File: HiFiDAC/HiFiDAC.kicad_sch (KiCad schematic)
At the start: 1 part, among them U2 PCM1794A

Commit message: HiFiDAC progress
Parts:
- added C27, C28, C29, C30, C31, C32: 47µF 20V, symbol Device:C_Polarized_Small
- added C33, C34, C35, C36: 0.1µF C0G, symbol Device:C_Small
- added C37: 1µF, symbol Device:C_Small
- added J1: I2S, symbol Connector:Conn_01x05_Pin
- added J2: Conn_01x04_Pin, symbol Connector:Conn_01x04_Pin
- added JP1: SolderJumper_2_Open, Jumper:SolderJumper-2_P1.3mm_Open_RoundedPad1.0x1.5mm, symbol Jumper:SolderJumper_2_Open
- added R31: 10kΩLN, symbol Device:R_US
- added R32: 10Ω, symbol Device:R_US
- added R33, R34, R35, R36, R38: 27Ω, symbol Device:R_US
- added R37: 1kΩ, symbol Device:R_US
- added R39: 100kΩ, symbol Device:R_US
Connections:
- net I-V Stage/IL+: now also U2.25 (IOUTL+)
- net I-V Stage/IL-: now also U2.26 (IOUTL-)
- net I-V Stage/IR+: now also U2.17 (IOUTR+)
- net I-V Stage/IR-: now also U2.18 (IOUTR-)
- net at U2.10 (MUTE): now also R36.2
- net ZERO: now reaches U2.13 (ZERO)
- net ZERO: now also R38.2
- net at U2.14 (~{RST}): now also C37.1, R37.2, R39.1
- net +5V: now reaches U2.15 (VCC2R)
- net +5V: now also U2.23 (VCC1), U2.28 (VCC2L), C27.1, C28.1, C29.1, C30.1, C31.1, C33.2, C34.2, C35.2
- net GND: now reaches U2.16 (AGND3R)
- net GND: now also U2.19 (AGND1), U2.24 (AGND2), U2.27 (AGND3L), U2.8 (DGND), C29.2, C30.2, C31.2, C32.2, C33.1, C34.1, C35.1, C36.2, C37.2, J1.1 (Pin_1), J2.4 (Pin_4), R31.2, R39.2
- net at U2.20 (IREF): now also R31.1
- net at U2.21 (VCOMR): now also C28.2
- net at U2.22 (VCOML): now also C27.2
- net at U2.4 (LRCK): now also R34.2
- net at U2.5 (DATA): now also R35.2
- net at U2.6 (BCK): now also R33.2
- net at U2.7 (SCK): now also R32.2
- net +3.3V: now reaches U2.9 (VDD)
- net +3.3V: now also C32.1, C36.1
- new net: J2.3 (Pin_3), R38.1
- new net: J1.4 (Pin_4), R34.1
- new net: J2.1 (Pin_1), R36.1
- new net: J2.2 (Pin_2), R37.1
- new net: J1.2 (Pin_2), R32.1
- new net: J1.3 (Pin_3), R33.1
- new net: J1.5 (Pin_5), R35.1
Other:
- moved on the sheet: U2

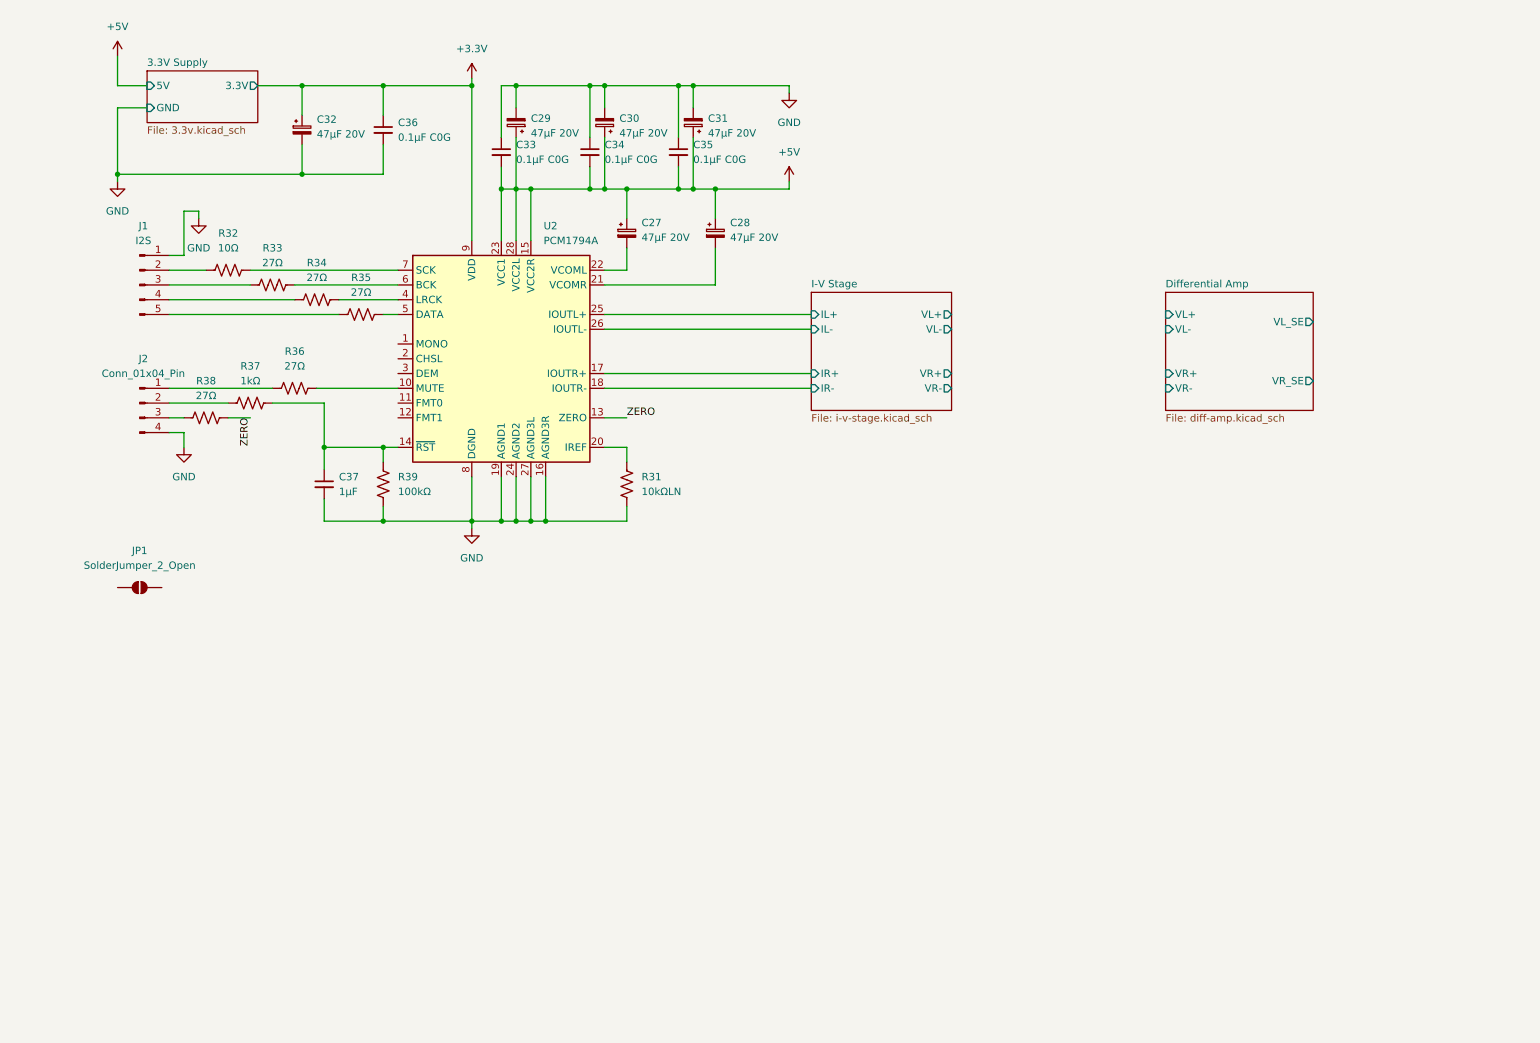
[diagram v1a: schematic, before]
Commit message: HiFiDAC schematic initially done, CleanLVSupply added shield pads
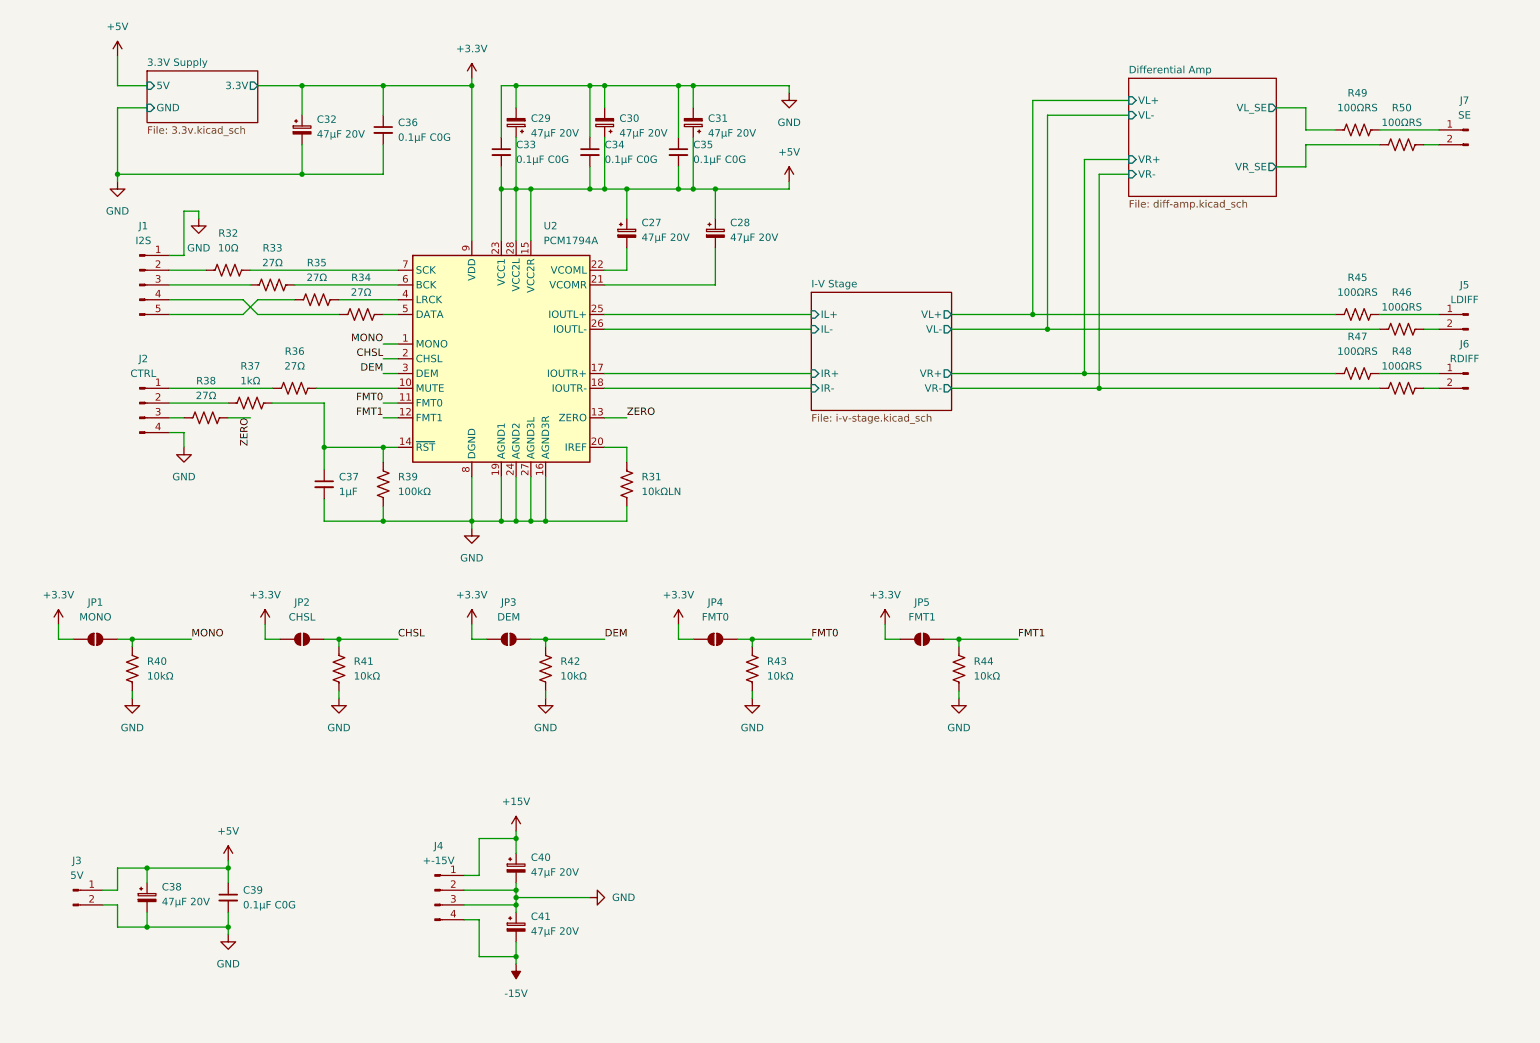
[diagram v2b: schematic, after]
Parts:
- added C38, C40, C41: 47µF 20V, symbol Device:C_Polarized_Small
- added C39: 0.1µF C0G, symbol Device:C_Small
- added J3: 5V, symbol Connector:Conn_01x02_Pin
- added J4: +-15V, symbol Connector:Conn_01x04_Pin
- added J5: LDIFF, symbol Connector:Conn_01x02_Pin
- added J6: RDIFF, symbol Connector:Conn_01x02_Pin
- added J7: SE, symbol Connector:Conn_01x02_Pin
- added JP2: CHSL, Jumper:SolderJumper-2_P1.3mm_Open_RoundedPad1.0x1.5mm, symbol Jumper:SolderJumper_2_Open
- added JP3: DEM, Jumper:SolderJumper-2_P1.3mm_Open_RoundedPad1.0x1.5mm, symbol Jumper:SolderJumper_2_Open
- added JP4: FMT0, Jumper:SolderJumper-2_P1.3mm_Open_RoundedPad1.0x1.5mm, symbol Jumper:SolderJumper_2_Open
- added JP5: FMT1, Jumper:SolderJumper-2_P1.3mm_Open_RoundedPad1.0x1.5mm, symbol Jumper:SolderJumper_2_Open
- added R40, R41, R42, R43, R44: 10kΩ, symbol Device:R_US
- added R45, R46, R47, R48, R49, R50: 100ΩRS, symbol Device:R_US
- J2: value Conn_01x04_Pin -> CTRL
- JP1: value SolderJumper_2_Open -> MONO
- renumbered R35 to R34, R34 to R35
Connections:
- net +3.3V: now also JP1.1 (A), JP2.1 (A), JP3.1 (A), JP4.1 (A), JP5.1 (A)
- net +5V: now also C38.1, C39.1, J3.1 (Pin_1)
- net Differential Amp/VL+: now also R45.2
- net Differential Amp/VL-: now also R46.2
- net Differential Amp/VL_SE: now also R49.2
- net Differential Amp/VR+: now also R47.2
- net Differential Amp/VR-: now also R48.2
- net Differential Amp/VR_SE: now also R50.2
- net GND: now also C38.2, C39.2, C40.2, C41.1, J3.2 (Pin_2), J4.2 (Pin_2), J4.3 (Pin_3), R40.2, R41.2, R42.2, R43.2, R44.2
- net MONO: now reaches JP1.2 (B)
- net MONO: now also U2.1 (MONO), R40.1
- net at R35.1: now also J1.5 (Pin_5); no longer J1.4 (Pin_4)
- net at R34.1: now also J1.4 (Pin_4); no longer J1.5 (Pin_5)
- net FMT0: now reaches U2.11 (FMT0)
- net FMT0: now also JP4.2 (B), R43.1
- net FMT1: now reaches U2.12 (FMT1)
- net FMT1: now also JP5.2 (B), R44.1
- net CHSL: now reaches U2.2 (CHSL)
- net CHSL: now also JP2.2 (B), R41.1
- net DEM: now reaches U2.3 (DEM)
- net DEM: now also JP3.2 (B), R42.1
- new net: J5.1 (Pin_1), R45.1
- new net: J5.2 (Pin_2), R46.1
- new net: J6.1 (Pin_1), R47.1
- new net: J6.2 (Pin_2), R48.1
- new net: J7.1 (Pin_1), R49.1
- new net: J7.2 (Pin_2), R50.1
- new net +15V: C40.1, J4.1 (Pin_1)
- new net -15V: C41.2, J4.4 (Pin_4)
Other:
- moved on the sheet: JP1

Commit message: HiFiDAC renumbered and footprints assigned
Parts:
- C1: renamed from C29; footprint (none) -> Capacitor_SMD:CP_Elec_5x5.8
- C10: renamed from C28; footprint (none) -> Capacitor_SMD:CP_Elec_5x5.8
- C11: renamed from C37; footprint (none) -> Capacitor_SMD:C_0603_1608Metric
- C12: renamed from C40; footprint (none) -> Capacitor_SMD:CP_Elec_5x5.8
- C13: renamed from C38; footprint (none) -> Capacitor_SMD:CP_Elec_5x5.8
- C14: renamed from C39; footprint (none) -> BW_PassiveMechanical:C_0704_1810Metric
- C15: renamed from C41; footprint (none) -> Capacitor_SMD:CP_Elec_5x5.8
- C2: renamed from C30; footprint (none) -> Capacitor_SMD:CP_Elec_5x5.8
- C3: renamed from C31; footprint (none) -> Capacitor_SMD:CP_Elec_5x5.8
- C4: renamed from C32; footprint (none) -> Capacitor_SMD:CP_Elec_5x5.8
- C5: renamed from C36; footprint (none) -> BW_PassiveMechanical:C_0704_1810Metric
- C6: renamed from C33; footprint (none) -> BW_PassiveMechanical:C_0704_1810Metric
- C7: renamed from C34; footprint (none) -> BW_PassiveMechanical:C_0704_1810Metric
- C8: renamed from C35; footprint (none) -> BW_PassiveMechanical:C_0704_1810Metric
- C9: renamed from C27; footprint (none) -> Capacitor_SMD:CP_Elec_5x5.8
- J1: renamed from J7; footprint (none) -> BW_Connectors:Amphenol_MINITEK_0.8_2P_V
- J2: renamed from J1; footprint (none) -> BW_Connectors:Amphenol_MINITEK_0.8_5P_V
- J3: renamed from J5; footprint (none) -> BW_Connectors:Amphenol_MINITEK_0.8_2P_V
- J4: renamed from J6; footprint (none) -> BW_Connectors:Amphenol_MINITEK_0.8_2P_V
- J5: renamed from J2; footprint (none) -> BW_Connectors:Amphenol_MINITEK_0.8_4P_V
- J6: renamed from J3; footprint (none) -> BW_Connectors:Amphenol_MINITEK_0.8_2P_V
- J7: renamed from J4; footprint (none) -> BW_Connectors:Amphenol_MINITEK_0.8_4P_V
- R1: renamed from R49; footprint (none) -> Resistor_SMD:R_0805_2012Metric
- R10: renamed from R36; footprint (none) -> Resistor_SMD:R_0603_1608Metric
- R11: renamed from R48; footprint (none) -> Resistor_SMD:R_0805_2012Metric
- R12: renamed from R37; footprint (none) -> Resistor_SMD:R_0603_1608Metric
- R13: renamed from R38; footprint (none) -> Resistor_SMD:R_0603_1608Metric
- R14: renamed from R39; footprint (none) -> Resistor_SMD:R_0603_1608Metric
- R15: renamed from R31; footprint (none) -> Resistor_SMD:R_0603_1608Metric
- R16: renamed from R40; footprint (none) -> Resistor_SMD:R_0603_1608Metric
- R17: renamed from R41; footprint (none) -> Resistor_SMD:R_0603_1608Metric
- R18: renamed from R42; footprint (none) -> Resistor_SMD:R_0603_1608Metric
- R19: renamed from R43; footprint (none) -> Resistor_SMD:R_0603_1608Metric
- R2: renamed from R50; footprint (none) -> Resistor_SMD:R_0805_2012Metric
- R20: renamed from R44; footprint (none) -> Resistor_SMD:R_0603_1608Metric
- R3: renamed from R32; footprint (none) -> Resistor_SMD:R_0603_1608Metric
- R4: renamed from R33; footprint (none) -> Resistor_SMD:R_0603_1608Metric
- R5: renamed from R35; footprint (none) -> Resistor_SMD:R_0603_1608Metric
- R6: renamed from R34; footprint (none) -> Resistor_SMD:R_0603_1608Metric
- R7: renamed from R45; footprint (none) -> Resistor_SMD:R_0805_2012Metric
- R8: renamed from R46; footprint (none) -> Resistor_SMD:R_0805_2012Metric
- R9: renamed from R47; footprint (none) -> Resistor_SMD:R_0805_2012Metric
- renumbered U2 to U1

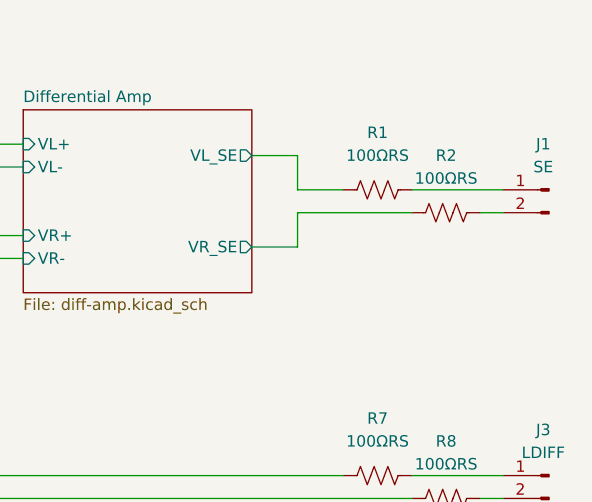
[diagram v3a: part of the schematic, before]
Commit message: HiFiDAC PCB progress, slight shape changes
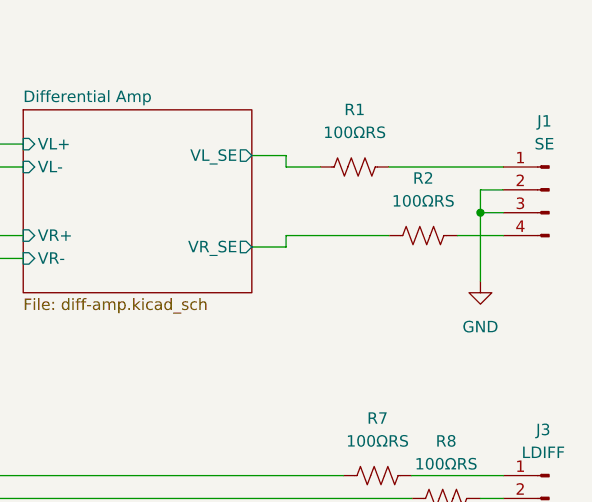
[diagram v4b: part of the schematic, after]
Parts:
- J1: footprint BW_Connectors:Amphenol_MINITEK_0.8_2P_V -> BW_Connectors:Amphenol_MINITEK_0.8_4P_V; symbol Connector:Conn_01x02_Pin -> Connector:Conn_01x04_Pin
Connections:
- net GND: now also J1.2 (Pin_2), J1.3 (Pin_3)
- net at R2.1: now also J1.4 (Pin_4); no longer J1.2 (Pin_2)
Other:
- moved on the sheet: R1, R2
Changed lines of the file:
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@@
 	)
 	(junction
+		(at 264.16 39.37)
+		(diameter 0)
+		(color 0 0 0 0)
+	)
+	(junction
 		(at 120.65 29.21)
 		(diameter 0)
@@
 	(wire
 		(pts
-			(xy 243.84 36.83) (xy 243.84 33.02)
+			(xy 242.57 34.29) (xy 242.57 33.02)
 		)
 		(stroke
@@
 	(wire
 		(pts
+			(xy 264.16 39.37) (xy 264.16 46.99)
+		)
+		(stroke
+			(width 0)
+			(type default)
+		)
+	)
+	(wire
+		(pts
 			(xy 101.6 172.72) (xy 101.6 179.07)
 		)
@@
 	(wire
 		(pts
+			(xy 261.62 41.91) (xy 266.7 41.91)
+		)
+		(stroke
+			(width 0)
+			(type default)
+		)
+	)
+	(wire
+		(pts
 			(xy 107.95 29.21) (xy 107.95 33.02)
 		)
@@
 	(wire
 		(pts
-			(xy 58.42 162.56) (xy 58.42 163.83)
+			(xy 266.7 36.83) (xy 264.16 36.83)
 		)
 		(stroke
@@
 	(wire
 		(pts
-			(xy 120.65 43.18) (xy 120.65 46.99)
+			(xy 58.42 162.56) (xy 58.42 163.83)
 		)
 		(stroke
@@
 	(wire
 		(pts
-			(xy 264.16 39.37) (xy 266.7 39.37)
+			(xy 120.65 43.18) (xy 120.65 46.99)
 		)
 		(stroke
@@
 	(wire
 		(pts
-			(xy 248.92 36.83) (xy 243.84 36.83)
+			(xy 246.38 34.29) (xy 242.57 34.29)
 		)
 		(stroke
@@
 	(wire
 		(pts
+			(xy 264.16 39.37) (xy 266.7 39.37)
+		)
+		(stroke
+			(width 0)
+			(type default)
+		)
+	)
+	(wire
+		(pts
 			(xy 105.41 46.99) (xy 105.41 55.88)
 		)
@@
 	(wire
 		(pts
+			(xy 264.16 36.83) (xy 264.16 39.37)
+		)
+		(stroke
+			(width 0)
+			(type default)
+		)
+	)
+	(wire
+		(pts
 			(xy 100.33 121.92) (xy 100.33 124.46)
 		)
@@
 	(wire
 		(pts
-			(xy 243.84 39.37) (xy 256.54 39.37)
+			(xy 242.57 41.91) (xy 254 41.91)
 		)
 		(stroke
@@
 	(wire
 		(pts
-			(xy 238.76 43.18) (xy 243.84 43.18)
+			(xy 238.76 43.18) (xy 242.57 43.18)
 		)
 		(stroke
@@
 	(wire
 		(pts
-			(xy 256.54 36.83) (xy 266.7 36.83)
-		)
-		(stroke
-			(width 0)
-			(type default)
-		)
-	)
-	(wire
-		(pts
 			(xy 100.33 104.14) (xy 105.41 104.14)
 		)
@@
 	(wire
 		(pts
-			(xy 243.84 43.18) (xy 243.84 39.37)
+			(xy 242.57 43.18) (xy 242.57 41.91)
 		)
 		(stroke
@@
 	(wire
 		(pts
+			(xy 254 34.29) (xy 266.7 34.29)
+		)
+		(stroke
+			(width 0)
+			(type default)
+		)
+	)
+	(wire
+		(pts
 			(xy 135.89 121.92) (xy 135.89 124.46)
 		)
@@
 	(wire
 		(pts
-			(xy 243.84 33.02) (xy 238.76 33.02)
+			(xy 242.57 33.02) (xy 238.76 33.02)
 		)
 		(stroke
@@
 	)
 	(symbol
+		(lib_id "power:GND")
+		(at 264.16 46.99 0)
+		(unit 1)
+		(exclude_from_sim no)
+		(in_bom yes)
+		(on_board yes)
+		(dnp no)
+		(fields_autoplaced yes)
+		(property "Reference" "#PWR045"
+			(at 264.16 53.34 0)
+			(effects
+				(font
+					(size 1.27 1.27)
+				)
+				(hide yes)
+			)
+		)
+		(property "Value" "GND"
+			(at 264.16 52.07 0)
+			(effects
+				(font
+					(size 1.27 1.27)
+				)
+			)
+		)
+		(property "Footprint" ""
+			(at 264.16 46.99 0)
+			(effects
+				(font
+					(size 1.27 1.27)
+				)
+				(hide yes)
+			)
+		)
+		(property "Datasheet" ""
+			(at 264.16 46.99 0)
+			(effects
+				(font
+					(size 1.27 1.27)
+				)
+				(hide yes)
+			)
+		)
+		(property "Description" "Power symbol creates a global label with name \"GND\" , ground"
+			(at 264.16 46.99 0)
+			(effects
+				(font
+					(size 1.27 1.27)
+				)
+				(hide yes)
+			)
+		)
+		(pin "1"
+		)
+		(instances
+			(project "HiFiDAC"
+				(path "/9ca5e549-4577-422c-b8f3-d4e6ad408ec3"
+					(reference "#PWR045")
+					(unit 1)
+				)
+			)
+		)
+	)
+	(symbol
 		(lib_id "Connector:Conn_01x02_Pin")
 		(at 31.75 167.64 0)
@@
 	)
 	(symbol
-		(lib_id "Connector:Conn_01x02_Pin")
+		(lib_id "Connector:Conn_01x04_Pin")
 		(at 271.78 36.83 0)
 		(mirror y)
@@
 		(dnp no)
 		(property "Reference" "J1"
-			(at 271.145 31.75 0)
+			(at 271.272 29.21 0)
 			(effects
 				(font
@@
 		)
 		(property "Value" "SE"
-			(at 271.145 34.29 0)
+			(at 271.272 31.75 0)
 			(effects
 				(font
@@
 			)
 		)
-		(property "Footprint" "BW_Connectors:Amphenol_MINITEK_0.8_2P_V"
+		(property "Footprint" "BW_Connectors:Amphenol_MINITEK_0.8_4P_V"
 			(at 271.78 36.83 0)
 			(effects
@@
 			)
 		)
-		(property "Description" "Generic connector, single row, 01x02, script generated"
+		(property "Description" "Generic connector, single row, 01x04, script generated"
 			(at 271.78 36.83 0)
 			(effects
@@
 		(pin "2"
 		)
+		(pin "3"
+		)
+		(pin "4"
+		)
 		(instances
 			(project "HiFiDAC"
@@
 	(symbol
 		(lib_id "Device:R_US")
-		(at 252.73 36.83 270)
+		(at 250.19 34.29 270)
 		(unit 1)
 		(exclude_from_sim no)
@@
 		(fields_autoplaced yes)
 		(property "Reference" "R1"
-			(at 252.73 30.48 90)
+			(at 250.19 27.94 90)
 			(effects
 				(font
@@
 		)
 		(property "Value" "100ΩRS"
-			(at 252.73 33.02 90)
+			(at 250.19 30.48 90)
 			(effects
 				(font
@@
 		)
 		(property "Footprint" "Resistor_SMD:R_0805_2012Metric"
-			(at 252.476 37.846 90)
+			(at 249.936 35.306 90)
 			(effects
 				(font
@@
 		)
 		(property "Datasheet" "~"
-			(at 252.73 36.83 0)
+			(at 250.19 34.29 0)
 			(effects
 				(font
@@
 		)
 		(property "Description" "Resistor, US symbol"
-			(at 252.73 36.83 0)
+			(at 250.19 34.29 0)
 			(effects
 				(font
@@
 	(symbol
 		(lib_id "Device:R_US")
-		(at 260.35 39.37 270)
+		(at 257.81 41.91 270)
 		(unit 1)
 		(exclude_from_sim no)
@@
 		(fields_autoplaced yes)
 		(property "Reference" "R2"
-			(at 260.35 33.02 90)
+			(at 257.81 35.56 90)
 			(effects
 				(font
@@
 		)
 		(property "Value" "100ΩRS"
-			(at 260.35 35.56 90)
+			(at 257.81 38.1 90)
 			(effects
 				(font
@@
 		)
 		(property "Footprint" "Resistor_SMD:R_0805_2012Metric"
-			(at 260.096 40.386 90)
+			(at 257.556 42.926 90)
 			(effects
 				(font
@@
 		)
 		(property "Datasheet" "~"
-			(at 260.35 39.37 0)
+			(at 257.81 41.91 0)
 			(effects
 				(font
@@
 		)
 		(property "Description" "Resistor, US symbol"
-			(at 260.35 39.37 0)
+			(at 257.81 41.91 0)
 			(effects
 				(font
